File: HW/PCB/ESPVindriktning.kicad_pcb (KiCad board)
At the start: 2 copper layers, 38 x 75 mm, 107 parts, among them P101 TestPoint_Small, P102 TestPoint_Small, P103 TestPoint_Small, P104 TestPoint_Small, P105 TestPoint_Small, P106 TestPoint_Small, P107 TestPoint_Small, P108 TestPoint_Small, P109 TestPoint_Small, P110 TestPoint_Small, P111 TestPoint_Small, P112 TestPoint_Small, P113 TestPoint_Small, P114 TestPoint_Small, P115 TestPoint_Small, P116 TestPoint_Small, P117 TestPoint_Small, P118 TestPoint_Small, P119 TestPoint_Small, P120 TestPoint_Small, P121 TestPoint_Small, P122 TestPoint_Small, P123 TestPoint_Small, P124 TestPoint_Small, P125 TestPoint_Small, P126 TestPoint_Small, P127 TestPoint_Small, P128 TestPoint_Small, P129 TestPoint_Small, P130 TestPoint_Small, P131 TestPoint_Small, P132 TestPoint_Small, P133 TestPoint_Small, P134 TestPoint_Small, P135 TestPoint_Small, P136 TestPoint_Small, P137 TestPoint_Small, SW101 reset, SW102 boot, T101 BSS138, T102 BSS138, X101 USB_C, X102 WS2812, X105 Fan, X106 PM1006, X107 I2C, X108 UART

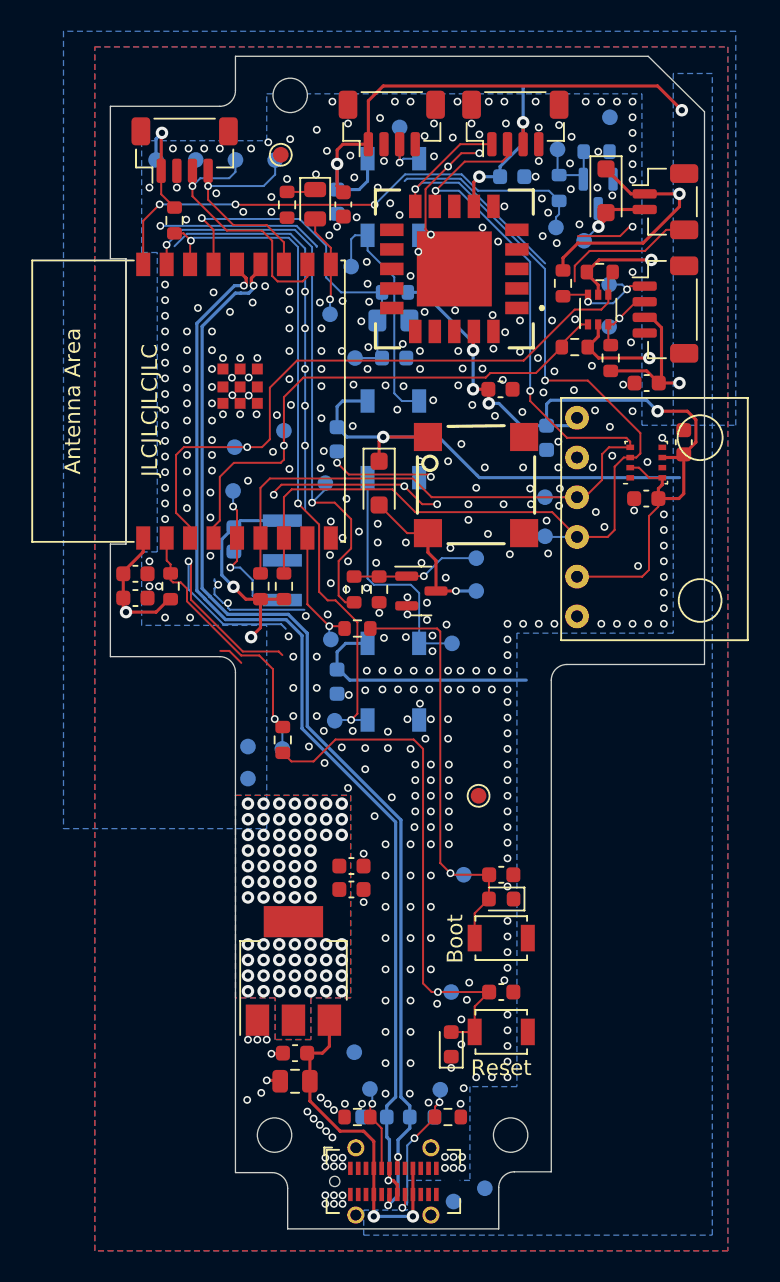
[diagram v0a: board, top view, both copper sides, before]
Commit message: Move ESP32 further into the PCB and replace IR receiver with smaller package
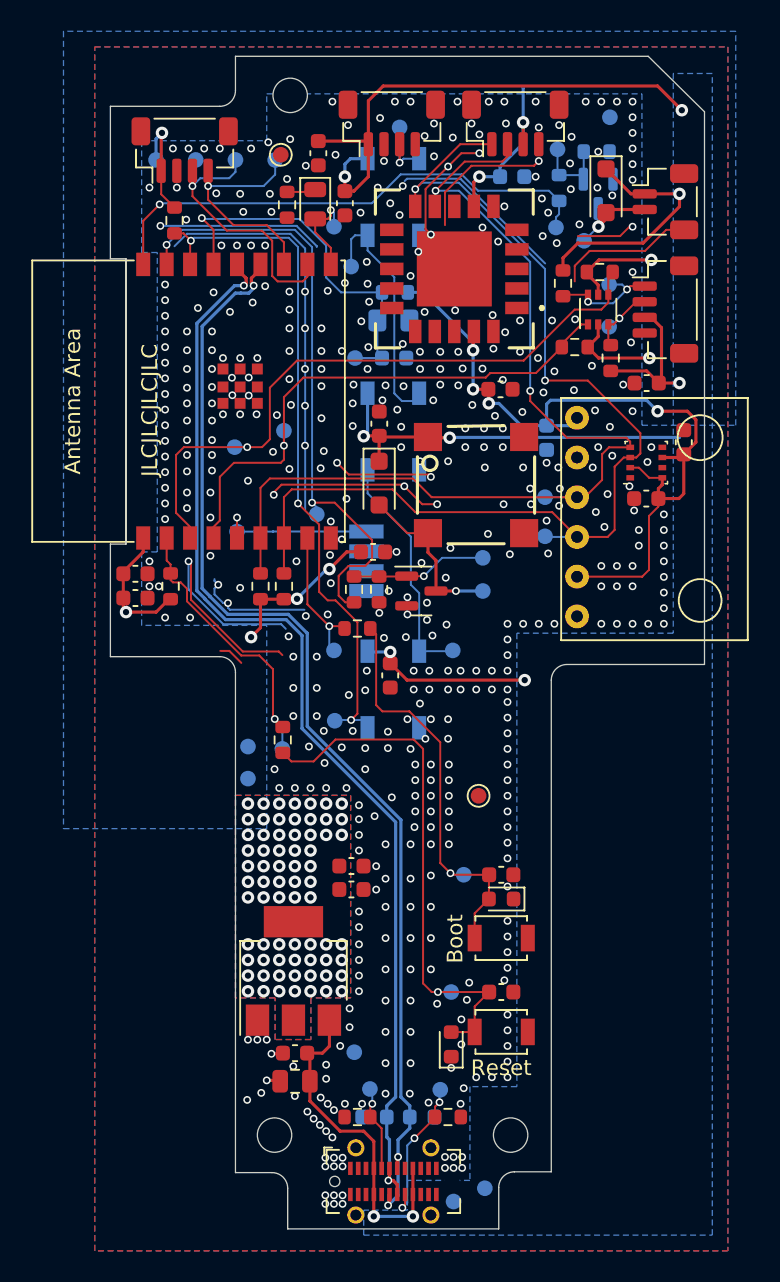
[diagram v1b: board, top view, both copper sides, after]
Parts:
- C103, C104, C107, C113: moved to F.Cu
- S103: value TSSP93038DF1PZA -> TSOP36238TT; footprint footprint:TSSP93038DF1PZA -> footprint:TSOP36238TT
- moved C113 8.94 mm to (108.8, 81.7), turned to 0 degrees
- moved P127 5.61 mm to (106.3, 60.9)
- moved C110 3.64 mm to (105.3, 56.2)
- moved C103 3.42 mm to (109.9, 89.6)
- moved C104 2.88 mm to (109.2, 73.5), turned to 90 degrees
- moved P123 2.61 mm to (100.1, 80.4)
- moved P109 2.07 mm to (105.2, 79.3)
- moved S103 1.73 mm to (108.4, 82.3)
- moved P126 0.73 mm to (106.3, 88.0)
- moved C107 0.51 mm to (107.0, 59.4)
- moved D105 0.50 mm to (110.1, 90.5)
- moved D106 0.50 mm to (110.1, 74.0)
- moved P103 0.45 mm to (113.9, 88.0)
- moved P132 0.42 mm to (115.8, 82.1)
- moved P133 0.42 mm to (115.8, 84.2)
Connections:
- S103 pad 1: /IR_OUT -> GND
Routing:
- net +5V: track 128.9 -> 118.2 mm, vias 7 -> 10
- net GND: track 115.5 -> 124.4 mm, vias 441 -> 474
- net +3.3V: track 103.8 -> 100.3 mm, vias 81 -> 82
- net Net-(D102-A2): track 28.1 -> 26.6 mm
- net /BUZZER: track 38.7 -> 39.7 mm
- net Net-(D105-DOUT): track 15.5 -> 14.6 mm
- net /BOOT: track 8.15 -> 8.93 mm
- net Net-(D110-A): track 6.53 -> 5.91 mm
- net /IR_OUT: track 9.95 -> 10.5 mm, vias 2 -> 1
- net /FAN: vias 3 -> 1

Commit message: Layout modifications to fit into housing
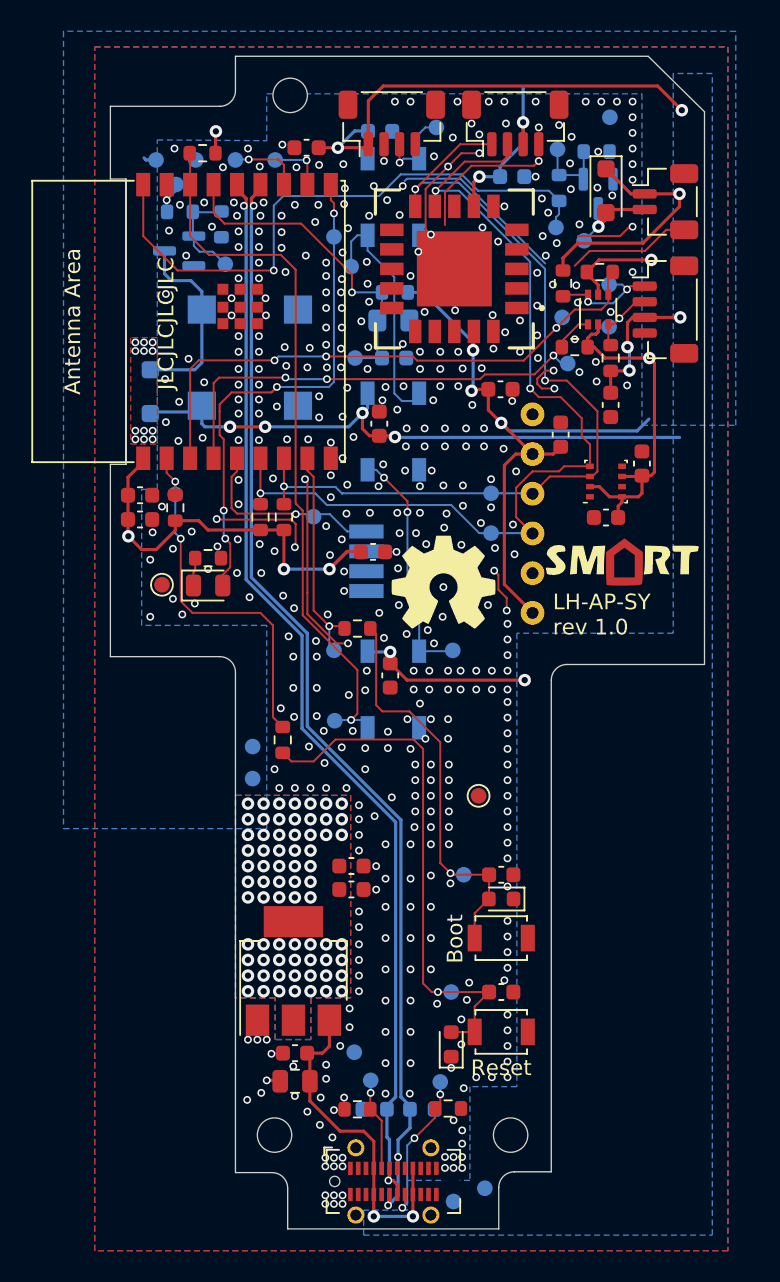
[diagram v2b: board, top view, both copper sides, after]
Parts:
- removed P133: TestPoint_Small, TestPoint:TestPoint_Pad_D1.0mm
- removed X108: UART, Connector_JST:JST_SH_BM04B-SRSS-TB_1x04-1MP_P1.00mm_Vertical
- added G***: LOGO, logo:logo, F.Cu at (124.8, 82.3)
- added G***: LOGO, LOGO, F.Cu at (124.8, 82.3)
- added REF**: OSHW-Symbol_6.7x6mm_Copper, Symbol:OSHW-Symbol_6.7x6mm_Copper, F.Cu at (113.3, 83.7)
- added REF**: OSHW-Symbol_6.7x6mm_SilkScreen, Symbol:OSHW-Symbol_6.7x6mm_SilkScreen, F.Cu at (113.3, 83.7)
- BZ101, C107, D108, R106, R108, S105, T101: moved to B.Cu
- C116: moved to F.Cu
- moved P113 28.5 mm to (95.3, 83.8)
- moved T101 26.7 mm to (96.4, 62.5), turned to 180 degrees
- moved R106 26.6 mm to (96.5, 60.0), turned to 0 degrees
- moved R108 25.4 mm to (99.1, 60.8)
- moved D110 25.3 mm to (98.2, 83.8), turned to 0 degrees
- moved P132 25.0 mm to (99.3, 63.3)
- moved R115 23.2 mm to (98.2, 82.1), turned to 180 degrees
- moved P109 22.9 mm to (96.2, 58.2)
- moved P117 22.5 mm to (120.9, 66.7)
- moved P122 18.7 mm to (121.2, 69.7)
- moved P106 17.7 mm to (96.2, 78.0)
- moved BZ101 16.6 mm to (100.9, 69.3)
- moved D108 15.8 mm to (94.5, 71.5), turned to 90 degrees
- moved S105 12.7 mm to (124.1, 73.2)
- moved C107 5.12 mm to (109.2, 54.8), turned to 0 degrees
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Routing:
- net GND: track 124.4 -> 65.8 mm, vias 474 -> 447
- net /BUZZER: track 39.7 -> 3.56 mm, vias 2 -> 1
- net Net-(D110-A): track 5.91 -> 32.7 mm, vias 1 -> 4
- net /TXD0: track 17.4 -> 3.60 mm
- net /I2C_SDA: track 69.7 -> 56.9 mm, vias 2 -> 3
- net +5V: track 118.2 -> 128.6 mm, vias 10 -> 14
- net /RXD0: track 14.8 -> 4.56 mm
- net +3.3V: track 100.3 -> 110.3 mm, vias 82 -> 92
- net /~{RESET}: track 18.3 -> 23.7 mm, vias 1 -> 2
- net /I2C_SCL: track 66.2 -> 60.8 mm, vias 2 -> 3
- net /FAN: track 33.1 -> 38.3 mm
- net /BOOT: track 8.93 -> 14.0 mm
- net /PM_TX: track 42.1 -> 37.3 mm, vias 1 -> 3
- net /PM_RX: track 35.1 -> 31.7 mm, vias 1 -> 3
- net /BRIGHT_VAL: track 24.1 -> 21.5 mm
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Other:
- outline, holes or cut-outs redrawn
- board text added: "LH-AP-SY rev 1.0"

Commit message: Added final touches to the layout
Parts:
- moved R116 10.7 mm to (113.2, 95.8), turned to -90 degrees
- moved P126 9.20 mm to (113.8, 93.2)
- moved R117 8.96 mm to (111.8, 95.8)
- moved P122 7.41 mm to (113.9, 70.6)
- moved D110 4.86 mm to (98.0, 79.0), turned to 90 degrees
- moved D101 4.53 mm to (117.0, 110.0), turned to 180 degrees
- moved R115 3.44 mm to (99.8, 79.0), turned to -90 degrees
- moved C113 2.76 mm to (106.2, 82.8), turned to -90 degrees
- moved D108 2.31 mm to (95.2, 69.2)
- moved C112 1.68 mm to (93.8, 79.8)
- moved C111 1.38 mm to (93.8, 78.2)
- moved P101 1.35 mm to (113.9, 108.5)
- moved C101 1.35 mm to (117.0, 108.5)
- moved P113 1.20 mm to (96.5, 83.8)
- moved P123 1.00 mm to (105.0, 80.5)
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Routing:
- net Net-(D102-A2): track 26.6 -> 12.9 mm
- net Net-(D101-A2): track 34.8 -> 21.4 mm
- net /BOOT: track 14.0 -> 25.9 mm
- net /~{RESET}: track 23.7 -> 31.4 mm
- net Net-(D110-A): track 32.7 -> 27.8 mm, vias 4 -> 2
- net /USB_D+: track 70.5 -> 73.7 mm
- net /IR_OUT: track 12.6 -> 15.4 mm
- net Net-(BZ101-+): track 12.4 -> 10.6 mm
- net GND: track 65.8 -> 67.6 mm, vias 447 -> 389
- net /BUZZER: track 3.56 -> 5.27 mm
- net +3.3V: track 110.3 -> 111.7 mm, vias 92 -> 81
- net /WS2812_DI: track 45.7 -> 44.9 mm
- net Net-(T102-G): track 5.12 -> 5.80 mm
- net +5V: track 128.6 -> 128.8 mm, vias 14 -> 12
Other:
- outline, holes or cut-outs redrawn
- board text added: "Fan"
- board text added: "I2C"
- board text added: "PM1006"
- board text added: "WS2812"
- board text added: "locked"
- board text removed: "LH-AP-SY rev 1.0"

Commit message: Add DMC code and S/N Fields
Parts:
- added G*** (x2): LOGO, LOGO, B.Cu at (124.4, 83.3)
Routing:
- net /USB_D+: track 73.7 -> 70.9 mm
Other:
- board text added: "S/N"

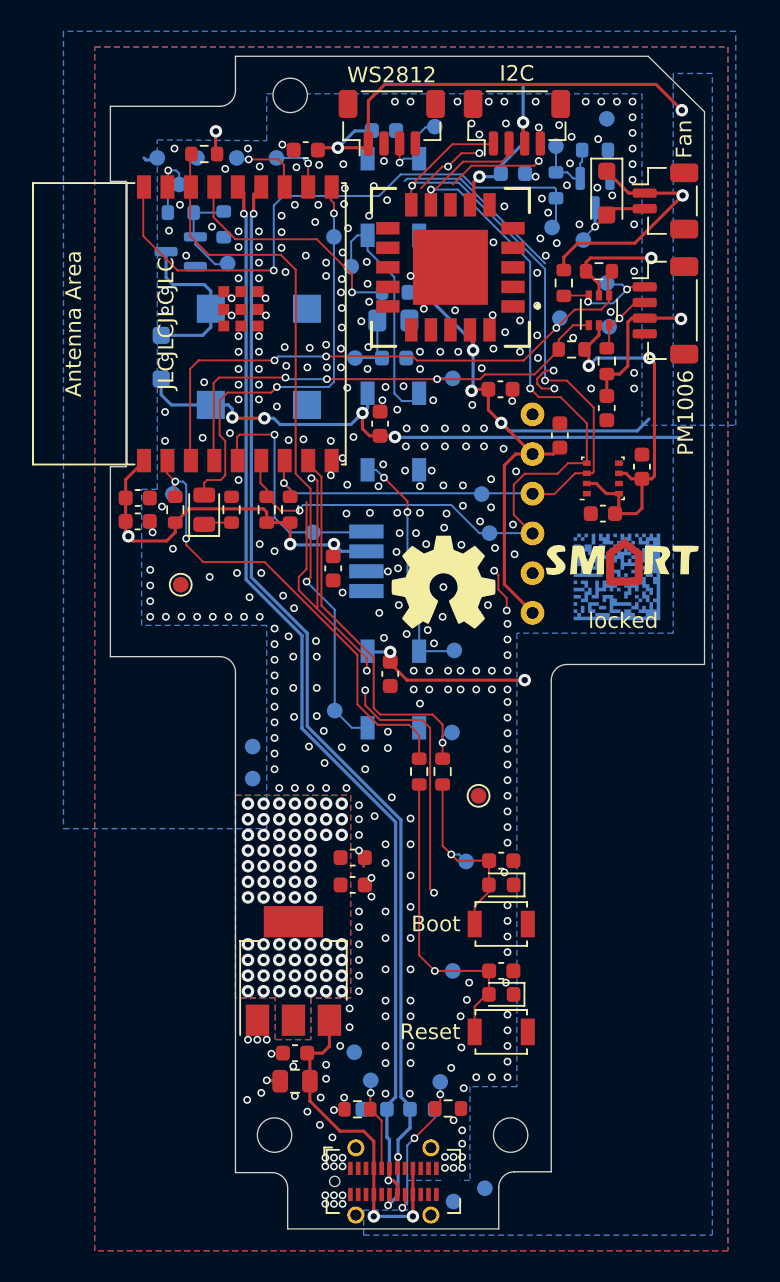
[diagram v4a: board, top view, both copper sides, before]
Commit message: Clean up schematic and layout further
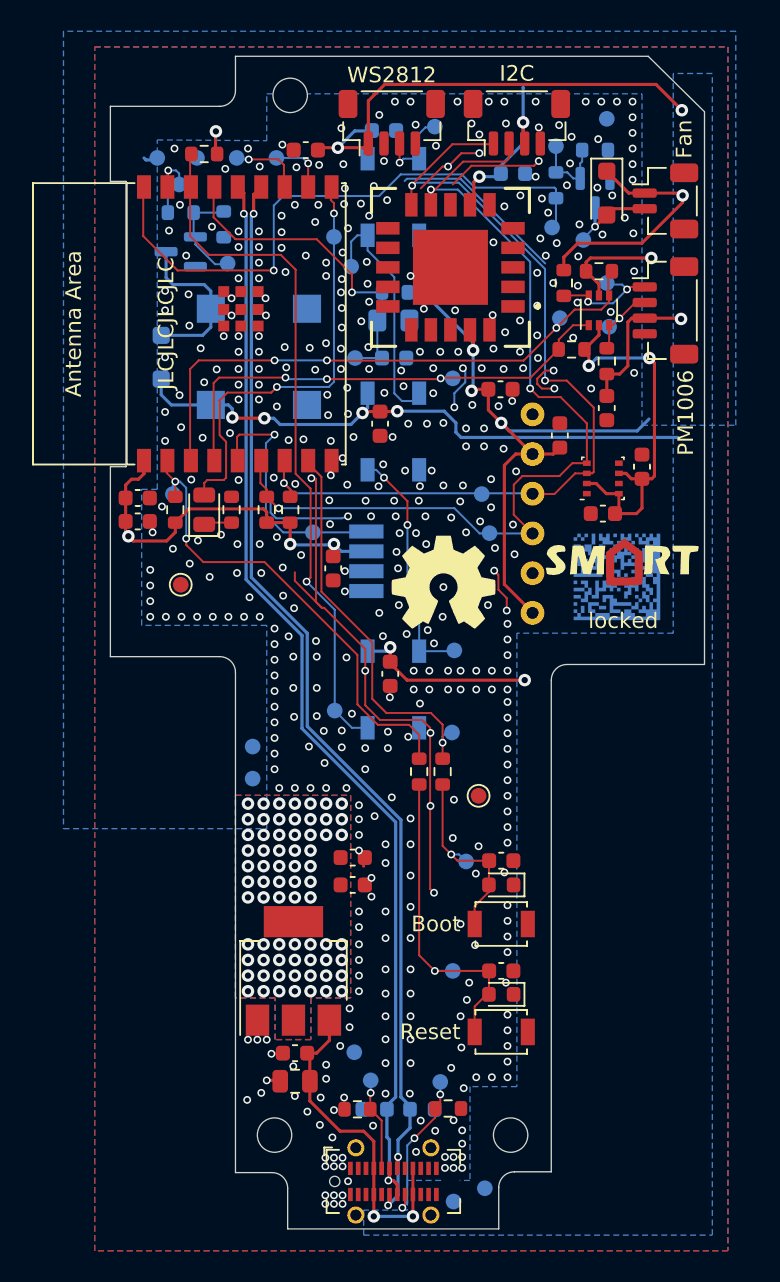
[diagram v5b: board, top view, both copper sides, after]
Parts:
- turned C104 to -90 degrees
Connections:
- net Net-(BZ101-+) renamed /BUZ_D
- net Net-(D101-A2) renamed /~{RST_BTN}
- net Net-(D102-A2) renamed /BOOT_BTN
- net Net-(D105-DOUT) renamed /WS2812_1_DO
- net Net-(D106-DOUT) renamed /WS2812_2_DO
- net Net-(D107-DOUT) renamed /WS2812_3_DO
- net Net-(D109-A) renamed /FAN_D
- net Net-(D110-A) renamed /STATUS_LED
- net Net-(D110-K) renamed /STATUS_LED_R
- net Net-(T101-G) renamed /BUZ_G
- net Net-(T102-G) renamed /FAN_G
- net Net-(X101-CC1) renamed /CC1
- net Net-(X101-CC2) renamed /CC2
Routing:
- net GND: track 67.6 -> 73.3 mm, vias 389 -> 441
- net +3.3V: track 111.7 -> 112.7 mm
- net /IR_OUT: track 15.4 -> 16.1 mm
